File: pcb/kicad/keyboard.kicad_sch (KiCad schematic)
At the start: 0 parts

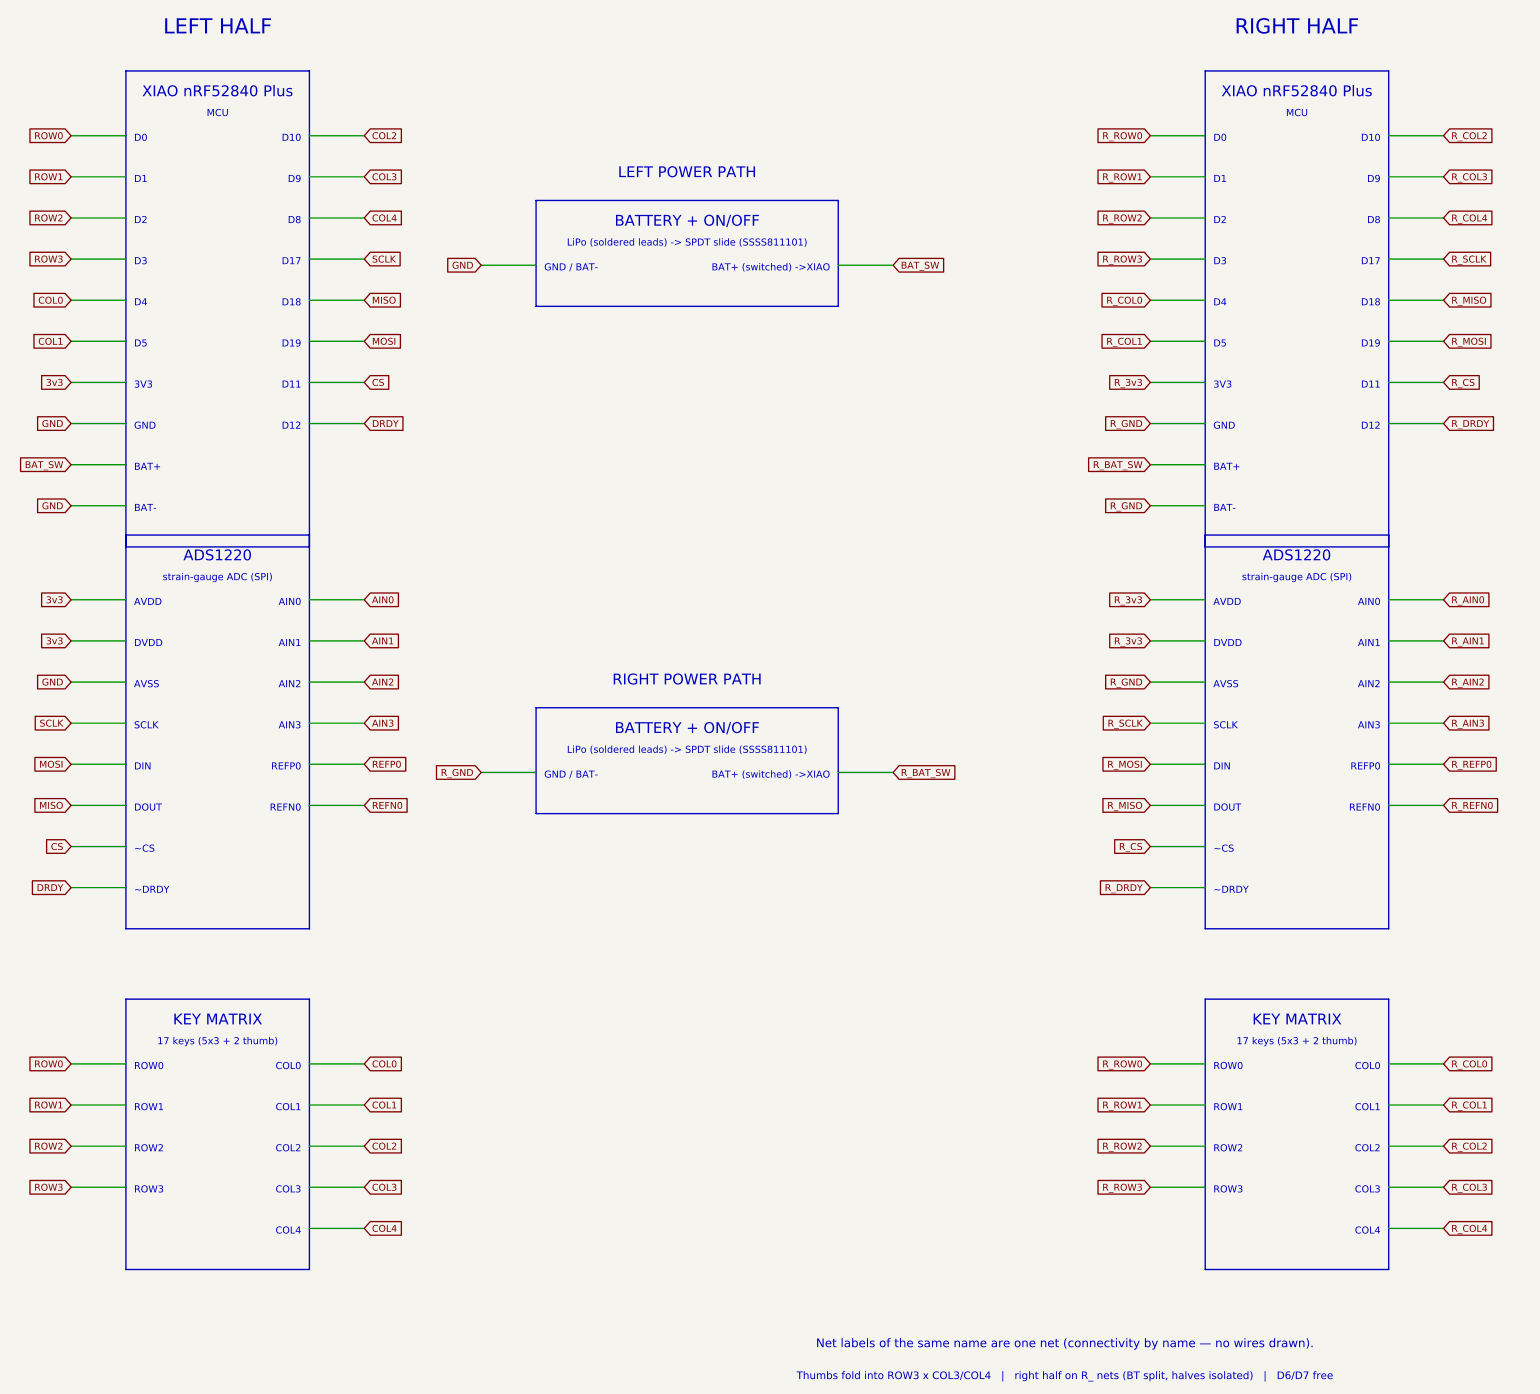
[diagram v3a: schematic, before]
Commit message: pcb(sch): add per-key RGB LED chain to net-map (XIAO D6 -> SK6812 x17)
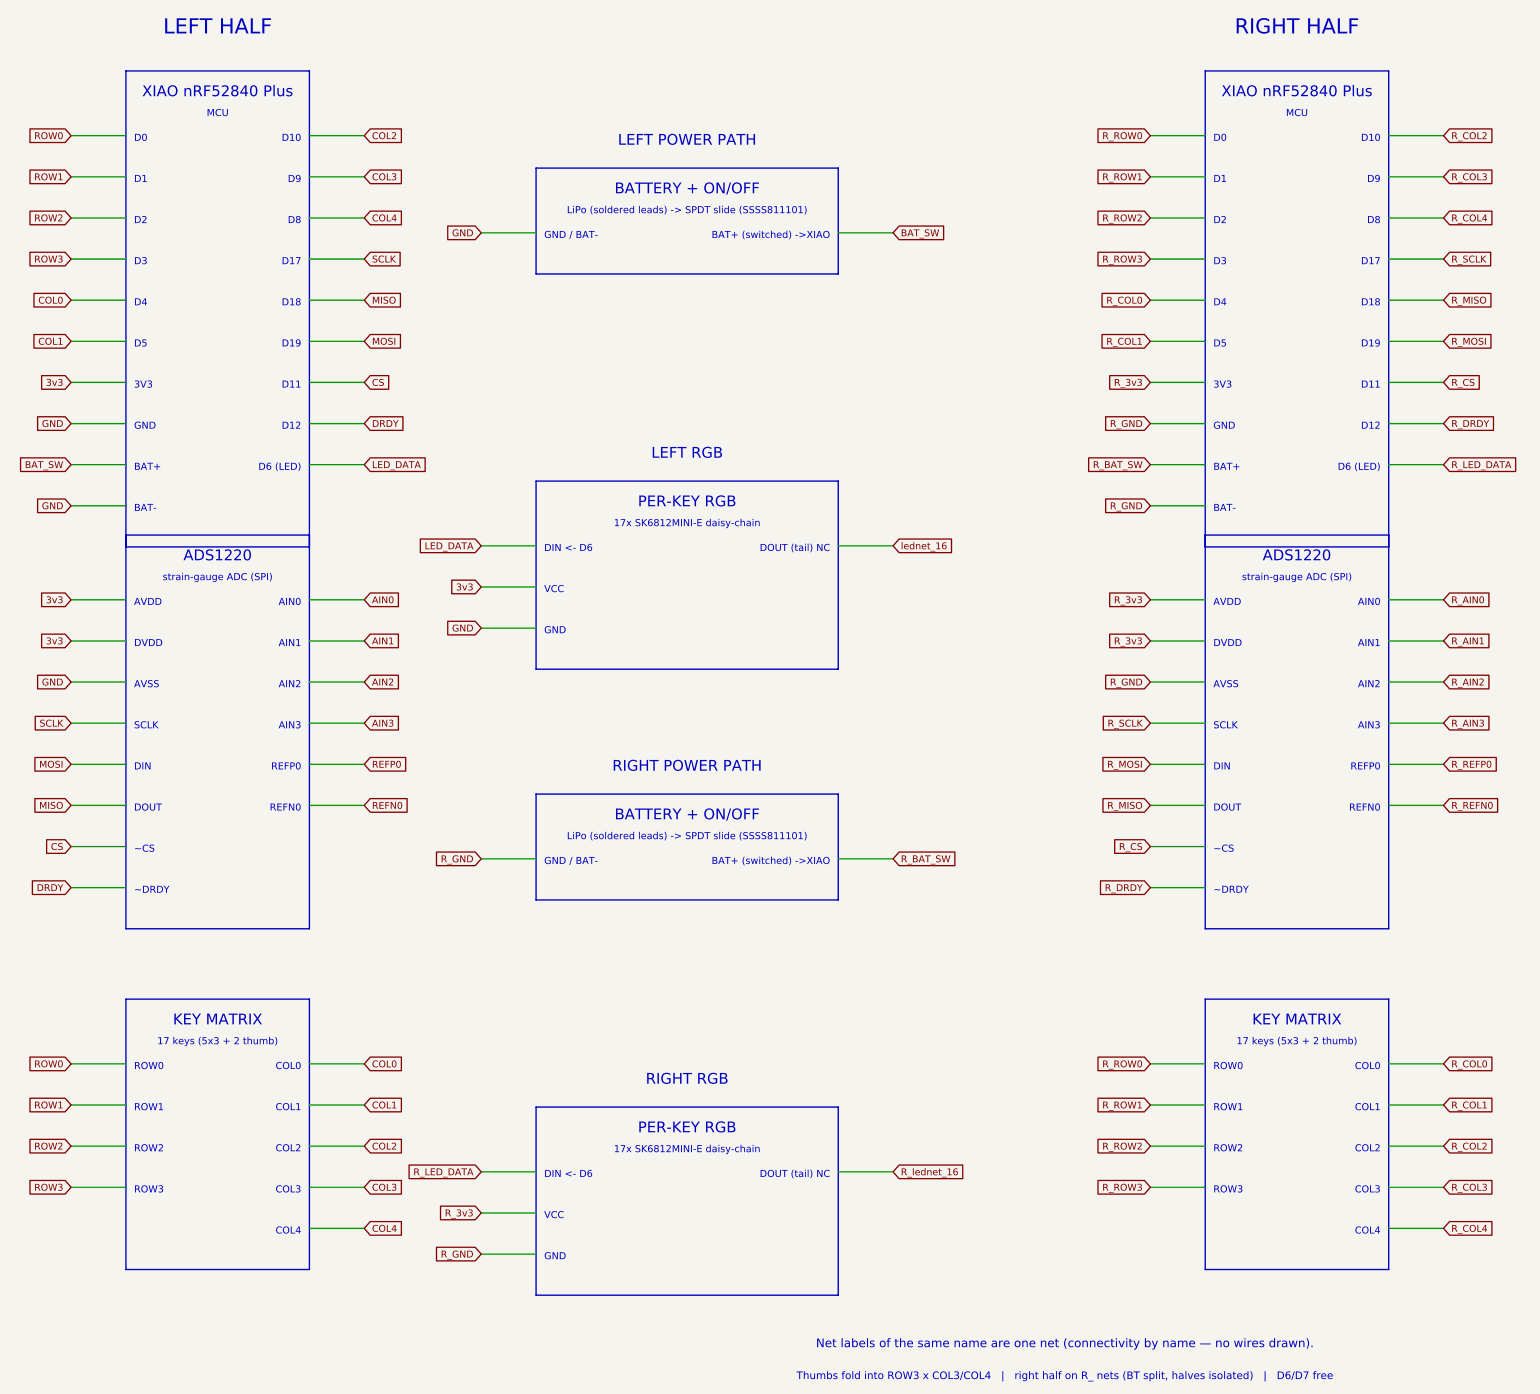
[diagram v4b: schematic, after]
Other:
- note added: "17x SK6812MINI-E daisy-chain"
- note added: "D6 (LED)"
- note added: "DIN <- D6"
- note added: "DOUT (tail) NC"
- note added: "LEFT RGB"
- note added: "PER-KEY RGB"
- note added: "RIGHT RGB"
- note added: "VCC"
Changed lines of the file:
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@@
 	(text "D12"(exclude_from_sim no)(at 68.5 97.94 0)
+    (effects (font (size 1.3 1.3))(justify right)))
+	(wire (pts (xy 70 104.96000000000001)(xy 80.16 104.96000000000001))(stroke (width 0.152)(type default)))
+	(global_label "LED_DATA"(shape input)(at 80.16 104.96000000000001 180)
+    (effects (font (size 1.27 1.27))(justify left)))
+	(text "D6 (LED)"(exclude_from_sim no)(at 68.5 105.56 0)
     (effects (font (size 1.3 1.3))(justify right)))
 	(rectangle (start 36 118)(end 70 190.96)
@@
 	(text "D12"(exclude_from_sim no)(at 268.5 97.94 0)
     (effects (font (size 1.3 1.3))(justify right)))
+	(wire (pts (xy 270 104.96000000000001)(xy 280.16 104.96000000000001))(stroke (width 0.152)(type default)))
+	(global_label "R_LED_DATA"(shape input)(at 280.16 104.96000000000001 180)
+    (effects (font (size 1.27 1.27))(justify left)))
+	(text "D6 (LED)"(exclude_from_sim no)(at 268.5 105.56 0)
+    (effects (font (size 1.3 1.3))(justify right)))
 	(rectangle (start 236 118)(end 270 190.96)
     (stroke (width 0.254)(type default))(fill (type background)))
@@
 	(text "COL4"(exclude_from_sim no)(at 268.5 247.07999999999998 0)
     (effects (font (size 1.3 1.3))(justify right)))
-	(text "LEFT POWER PATH"(exclude_from_sim no)(at 140 51 0)
-    (effects (font (size 2.0 2.0))))
-	(rectangle (start 112 56)(end 168 75.62)
-    (stroke (width 0.254)(type default))(fill (type background)))
-	(text "BATTERY + ON/OFF"(exclude_from_sim no)(at 140.0 60 0)
-    (effects (font (size 2.0 2.0))))
-	(text "LiPo (soldered leads) -> SPDT slide (SSSS811101)"(exclude_from_sim no)(at 140.0 64 0)
-    (effects (font (size 1.3 1.3))))
-	(wire (pts (xy 112 68.0)(xy 101.84 68.0))(stroke (width 0.152)(type default)))
-	(global_label "GND"(shape input)(at 101.84 68.0 0)
-    (effects (font (size 1.27 1.27))(justify right)))
-	(text "GND / BAT-"(exclude_from_sim no)(at 113.5 68.6 0)
-    (effects (font (size 1.3 1.3))(justify left)))
-	(wire (pts (xy 168 68.0)(xy 178.16 68.0))(stroke (width 0.152)(type default)))
-	(global_label "BAT_SW"(shape input)(at 178.16 68.0 180)
-    (effects (font (size 1.27 1.27))(justify left)))
-	(text "BAT+ (switched) ->XIAO"(exclude_from_sim no)(at 166.5 68.6 0)
-    (effects (font (size 1.3 1.3))(justify right)))
-	(text "RIGHT POWER PATH"(exclude_from_sim no)(at 140 145 0)
-    (effects (font (size 2.0 2.0))))
-	(rectangle (start 112 150)(end 168 169.62)
-    (stroke (width 0.254)(type default))(fill (type background)))
-	(text "BATTERY + ON/OFF"(exclude_from_sim no)(at 140.0 154 0)
-    (effects (font (size 2.0 2.0))))
-	(text "LiPo (soldered leads) -> SPDT slide (SSSS811101)"(exclude_from_sim no)(at 140.0 158 0)
-    (effects (font (size 1.3 1.3))))
-	(wire (pts (xy 112 162.0)(xy 101.84 162.0))(stroke (width 0.152)(type default)))
-	(global_label "R_GND"(shape input)(at 101.84 162.0 0)
-    (effects (font (size 1.27 1.27))(justify right)))
-	(text "GND / BAT-"(exclude_from_sim no)(at 113.5 162.6 0)
-    (effects (font (size 1.3 1.3))(justify left)))
-	(wire (pts (xy 168 162.0)(xy 178.16 162.0))(stroke (width 0.152)(type default)))
-	(global_label "R_BAT_SW"(shape input)(at 178.16 162.0 180)
-    (effects (font (size 1.27 1.27))(justify left)))
-	(text "BAT+ (switched) ->XIAO"(exclude_from_sim no)(at 166.5 162.6 0)
+	(text "LEFT POWER PATH"(exclude_from_sim no)(at 140 45 0)
+    (effects (font (size 2.0 2.0))))
+	(rectangle (start 112 50)(end 168 69.62)
+    (stroke (width 0.254)(type default))(fill (type background)))
+	(text "BATTERY + ON/OFF"(exclude_from_sim no)(at 140.0 54 0)
+    (effects (font (size 2.0 2.0))))
+	(text "LiPo (soldered leads) -> SPDT slide (SSSS811101)"(exclude_from_sim no)(at 140.0 58 0)
+    (effects (font (size 1.3 1.3))))
+	(wire (pts (xy 112 62.0)(xy 101.84 62.0))(stroke (width 0.152)(type default)))
+	(global_label "GND"(shape input)(at 101.84 62.0 0)
+    (effects (font (size 1.27 1.27))(justify right)))
+	(text "GND / BAT-"(exclude_from_sim no)(at 113.5 62.6 0)
+    (effects (font (size 1.3 1.3))(justify left)))
+	(wire (pts (xy 168 62.0)(xy 178.16 62.0))(stroke (width 0.152)(type default)))
+	(global_label "BAT_SW"(shape input)(at 178.16 62.0 180)
+    (effects (font (size 1.27 1.27))(justify left)))
+	(text "BAT+ (switched) ->XIAO"(exclude_from_sim no)(at 166.5 62.6 0)
+    (effects (font (size 1.3 1.3))(justify right)))
+	(text "LEFT RGB"(exclude_from_sim no)(at 140 103 0)
+    (effects (font (size 2.0 2.0))))
+	(rectangle (start 112 108)(end 168 142.86)
+    (stroke (width 0.254)(type default))(fill (type background)))
+	(text "PER-KEY RGB"(exclude_from_sim no)(at 140.0 112 0)
+    (effects (font (size 2.0 2.0))))
+	(text "17x SK6812MINI-E daisy-chain"(exclude_from_sim no)(at 140.0 116 0)
+    (effects (font (size 1.3 1.3))))
+	(wire (pts (xy 112 120.0)(xy 101.84 120.0))(stroke (width 0.152)(type default)))
+	(global_label "LED_DATA"(shape input)(at 101.84 120.0 0)
+    (effects (font (size 1.27 1.27))(justify right)))
+	(text "DIN <- D6"(exclude_from_sim no)(at 113.5 120.6 0)
+    (effects (font (size 1.3 1.3))(justify left)))
+	(wire (pts (xy 112 127.62)(xy 101.84 127.62))(stroke (width 0.152)(type default)))
+	(global_label "3v3"(shape input)(at 101.84 127.62 0)
+    (effects (font (size 1.27 1.27))(justify right)))
+	(text "VCC"(exclude_from_sim no)(at 113.5 128.22 0)
+    (effects (font (size 1.3 1.3))(justify left)))
+	(wire (pts (xy 112 135.24)(xy 101.84 135.24))(stroke (width 0.152)(type default)))
+	(global_label "GND"(shape input)(at 101.84 135.24 0)
+    (effects (font (size 1.27 1.27))(justify right)))
+	(text "GND"(exclude_from_sim no)(at 113.5 135.84 0)
+    (effects (font (size 1.3 1.3))(justify left)))
+	(wire (pts (xy 168 120.0)(xy 178.16 120.0))(stroke (width 0.152)(type default)))
+	(global_label "lednet_16"(shape input)(at 178.16 120.0 180)
+    (effects (font (size 1.27 1.27))(justify left)))
+	(text "DOUT (tail) NC"(exclude_from_sim no)(at 166.5 120.6 0)
+    (effects (font (size 1.3 1.3))(justify right)))
+	(text "RIGHT POWER PATH"(exclude_from_sim no)(at 140 161 0)
+    (effects (font (size 2.0 2.0))))
+	(rectangle (start 112 166)(end 168 185.62)
+    (stroke (width 0.254)(type default))(fill (type background)))
+	(text "BATTERY + ON/OFF"(exclude_from_sim no)(at 140.0 170 0)
+    (effects (font (size 2.0 2.0))))
+	(text "LiPo (soldered leads) -> SPDT slide (SSSS811101)"(exclude_from_sim no)(at 140.0 174 0)
+    (effects (font (size 1.3 1.3))))
+	(wire (pts (xy 112 178.0)(xy 101.84 178.0))(stroke (width 0.152)(type default)))
+	(global_label "R_GND"(shape input)(at 101.84 178.0 0)
+    (effects (font (size 1.27 1.27))(justify right)))
+	(text "GND / BAT-"(exclude_from_sim no)(at 113.5 178.6 0)
+    (effects (font (size 1.3 1.3))(justify left)))
+	(wire (pts (xy 168 178.0)(xy 178.16 178.0))(stroke (width 0.152)(type default)))
+	(global_label "R_BAT_SW"(shape input)(at 178.16 178.0 180)
+    (effects (font (size 1.27 1.27))(justify left)))
+	(text "BAT+ (switched) ->XIAO"(exclude_from_sim no)(at 166.5 178.6 0)
+    (effects (font (size 1.3 1.3))(justify right)))
+	(text "RIGHT RGB"(exclude_from_sim no)(at 140 219 0)
+    (effects (font (size 2.0 2.0))))
+	(rectangle (start 112 224)(end 168 258.86)
+    (stroke (width 0.254)(type default))(fill (type background)))
+	(text "PER-KEY RGB"(exclude_from_sim no)(at 140.0 228 0)
+    (effects (font (size 2.0 2.0))))
+	(text "17x SK6812MINI-E daisy-chain"(exclude_from_sim no)(at 140.0 232 0)
+    (effects (font (size 1.3 1.3))))
+	(wire (pts (xy 112 236.0)(xy 101.84 236.0))(stroke (width 0.152)(type default)))
+	(global_label "R_LED_DATA"(shape input)(at 101.84 236.0 0)
+    (effects (font (size 1.27 1.27))(justify right)))
+	(text "DIN <- D6"(exclude_from_sim no)(at 113.5 236.6 0)
+    (effects (font (size 1.3 1.3))(justify left)))
+	(wire (pts (xy 112 243.62)(xy 101.84 243.62))(stroke (width 0.152)(type default)))
+	(global_label "R_3v3"(shape input)(at 101.84 243.62 0)
+    (effects (font (size 1.27 1.27))(justify right)))
+	(text "VCC"(exclude_from_sim no)(at 113.5 244.22 0)
+    (effects (font (size 1.3 1.3))(justify left)))
+	(wire (pts (xy 112 251.24)(xy 101.84 251.24))(stroke (width 0.152)(type default)))
+	(global_label "R_GND"(shape input)(at 101.84 251.24 0)
+    (effects (font (size 1.27 1.27))(justify right)))
+	(text "GND"(exclude_from_sim no)(at 113.5 251.84 0)
+    (effects (font (size 1.3 1.3))(justify left)))
+	(wire (pts (xy 168 236.0)(xy 178.16 236.0))(stroke (width 0.152)(type default)))
+	(global_label "R_lednet_16"(shape input)(at 178.16 236.0 180)
+    (effects (font (size 1.27 1.27))(justify left)))
+	(text "DOUT (tail) NC"(exclude_from_sim no)(at 166.5 236.6 0)
     (effects (font (size 1.3 1.3))(justify right)))
 	(text "Net labels of the same name are one net (connectivity by name — no wires drawn)."(exclude_from_sim no)(at 210 268 0)
